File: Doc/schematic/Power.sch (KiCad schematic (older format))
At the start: 19 parts, among them K1 RELAY_1RT, K2 RELAY_1RT, P1 Power Board, P5 Trafo_IN_1, P6 Trafo_IN_2, P7 +24_PWR, Q1 BC548, U2 7805

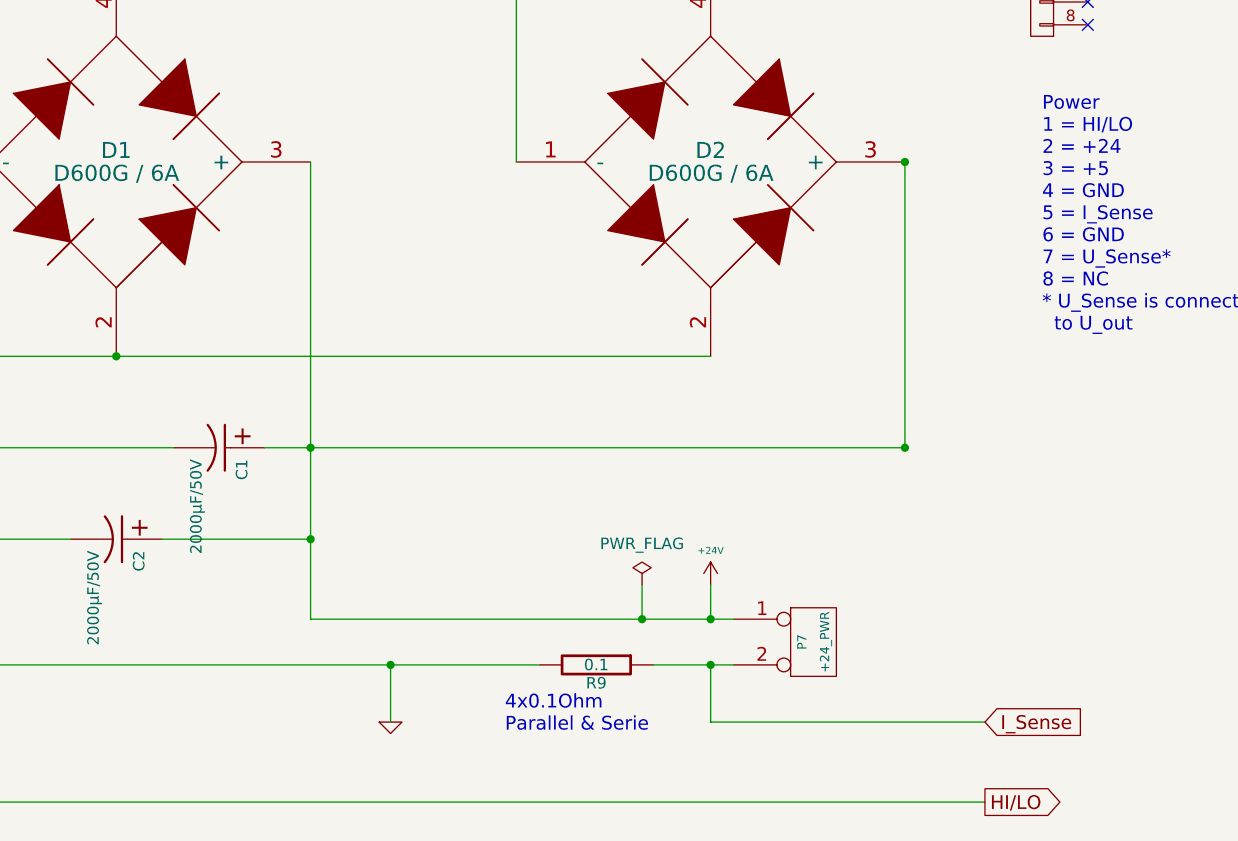
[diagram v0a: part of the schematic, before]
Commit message: Measurements and measurement-display first version finished.
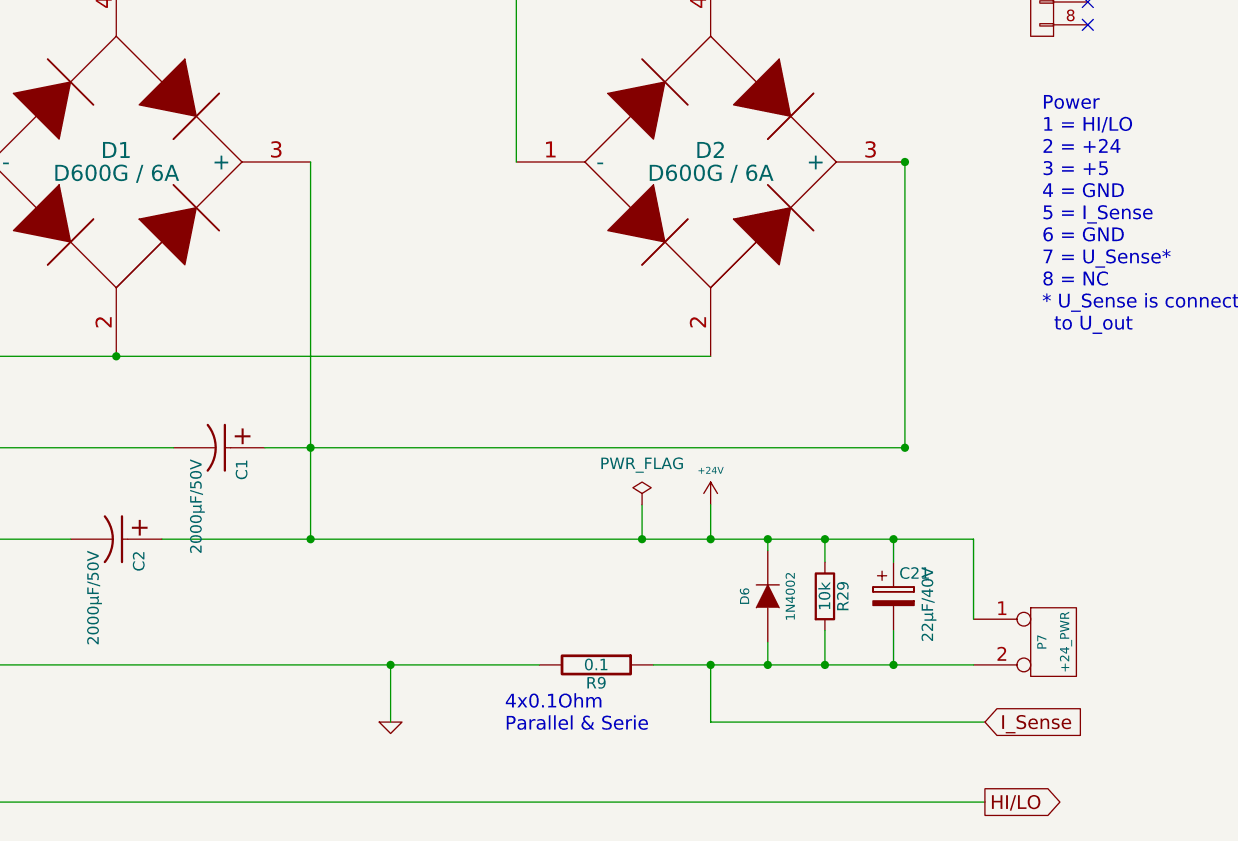
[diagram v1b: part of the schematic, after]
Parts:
- added C21: 22µF/40V, symbol CP
- added D6: 1N4002, symbol DIODE
- added R29: 10k, symbol R
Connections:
- net +24V: now also C21.1, D6.2 (K), R29.1
- net I_Sense: now also C21.2, D6.1 (A), R29.2
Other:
- moved on the sheet: P7
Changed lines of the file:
@@
 	9100 3350 9100 2100
 Wire Wire Line
-	6500 2100 6500 4100
+	6500 2100 6500 3750
 Wire Wire Line
 	4800 1150 4800 4300
@@
 	3350 1000 3350 1700
 Wire Wire Line
-	5850 3750 6500 3750
+	5850 3750 9400 3750
 Connection ~ 5650 1000
 Wire Wire Line
@@
 Wire Wire Line
 	6850 4550 6850 4300
-Wire Wire Line
-	6500 4100 8350 4100
 Wire Wire Line
 	1700 5400 2300 5400
@@
 Connection ~ 2100 2600
 Wire Wire Line
-	8000 4300 8350 4300
+	8000 4300 9400 4300
 Wire Wire Line
 	9450 4550 8250 4550
@@
 $EndComp
 $Comp
-L +24V #PWR22
+L +24V #PWR21
 U 1 1 50201F43
-P 8250 3950
-F 0 "#PWR22" H 8250 3900 20  0001 C CNN
-F 1 "+24V" H 8250 4100 30  0000 C CNN
-F 2 "" H 8250 3950 60  0001 C CNN
-F 3 "" H 8250 3950 60  0001 C CNN
-	1    8250 3950
+P 8250 3600
+F 0 "#PWR21" H 8250 3550 20  0001 C CNN
+F 1 "+24V" H 8250 3750 30  0000 C CNN
+F 2 "" H 8250 3600 60  0001 C CNN
+F 3 "" H 8250 3600 60  0001 C CNN
+	1    8250 3600
 	1    0    0    -1
 $EndComp
@@
 $EndComp
 $Comp
-L GND-RESCUE-Netzteil_Progammable #PWR21
+L GND-RESCUE-Netzteil_Progammable #PWR22
 U 1 1 50201970
 P 2100 3700
-F 0 "#PWR21" H 2100 3700 30  0001 C CNN
+F 0 "#PWR22" H 2100 3700 30  0001 C CNN
 F 1 "GND" H 2100 3630 30  0001 C CNN
 F 2 "" H 2100 3700 60  0001 C CNN
@@
 L CONN_2 P7
 U 1 1 50201731
-P 8700 4200
-F 0 "P7" V 8650 4200 40  0000 C CNN
-F 1 "+24_PWR" V 8750 4200 40  0000 C CNN
-F 2 "" H 8700 4200 60  0001 C CNN
-F 3 "" H 8700 4200 60  0001 C CNN
-	1    8700 4200
+P 9750 4200
+F 0 "P7" V 9700 4200 40  0000 C CNN
+F 1 "+24_PWR" V 9800 4200 40  0000 C CNN
+F 2 "" H 9750 4200 60  0001 C CNN
+F 3 "" H 9750 4200 60  0001 C CNN
+	1    9750 4200
 	1    0    0    -1
 $EndComp
@@
 L PWR_FLAG #FLG2
 U 1 1 589D1F88
-P 7950 3950
-F 0 "#FLG2" H 7950 4045 50  0001 C CNN
-F 1 "PWR_FLAG" H 7950 4130 50  0000 C CNN
-F 2 "" H 7950 3950 50  0000 C CNN
-F 3 "" H 7950 3950 50  0000 C CNN
-	1    7950 3950
+P 7950 3600
+F 0 "#FLG2" H 7950 3695 50  0001 C CNN
+F 1 "PWR_FLAG" H 7950 3780 50  0000 C CNN
+F 2 "" H 7950 3600 50  0000 C CNN
+F 3 "" H 7950 3600 50  0000 C CNN
+	1    7950 3600
 	1    0    0    -1
 $EndComp
@@
 I_Sense
 Wire Wire Line
-	8250 3950 8250 4100
-Connection ~ 8250 4100
-Wire Wire Line
-	7950 3950 7950 4100
-Connection ~ 7950 4100
+	8250 3750 8250 3600
+Connection ~ 8250 3750
+Wire Wire Line
+	7950 3600 7950 3750
+Connection ~ 7950 3750
 NoConn ~ 9900 1400
 Wire Wire Line
 	8750 5950 8750 6050
+Wire Wire Line
+	9400 3750 9400 4100
+$Comp
+L DIODE D6
+U 1 1 58FF4F3C
+P 8500 4000
+F 0 "D6" H 8500 4100 40  0000 C CNN
+F 1 "1N4002" H 8500 3900 40  0000 C CNN
+F 2 "" H 8500 4000 60  0000 C CNN
+F 3 "" H 8500 4000 60  0000 C CNN
+	1    8500 4000
+	0    -1   -1   0
+$EndComp
+$Comp
+L R R29
+U 1 1 58FF4FDD
+P 8750 4000
+F 0 "R29" V 8830 4000 50  0000 C CNN
+F 1 "10k" V 8750 4000 50  0000 C CNN
+F 2 "" V 8680 4000 50  0001 C CNN
+F 3 "" H 8750 4000 50  0001 C CNN
+	1    8750 4000
+	1    0    0    -1
+$EndComp
+$Comp
+L CP C21
+U 1 1 58FF5267
+P 9050 4000
+F 0 "C21" H 9075 4100 50  0000 L CNN
+F 1 "22µF/40V" V 9200 3800 50  0000 L CNN
+F 2 "" H 9088 3850 50  0001 C CNN
+F 3 "" H 9050 4000 50  0001 C CNN
+	1    9050 4000
+	1    0    0    -1
+$EndComp
+Wire Wire Line
+	9050 3850 9050 3750
+Connection ~ 9050 3750
+Wire Wire Line
+	8750 3850 8750 3750
+Connection ~ 8750 3750
+Wire Wire Line
+	8500 3800 8500 3750
+Connection ~ 8500 3750
+Wire Wire Line
+	8500 4200 8500 4300
+Connection ~ 8500 4300
+Wire Wire Line
+	8750 4150 8750 4300
+Connection ~ 8750 4300
+Wire Wire Line
+	9050 4150 9050 4300
+Connection ~ 9050 4300
 $EndSCHEMATC

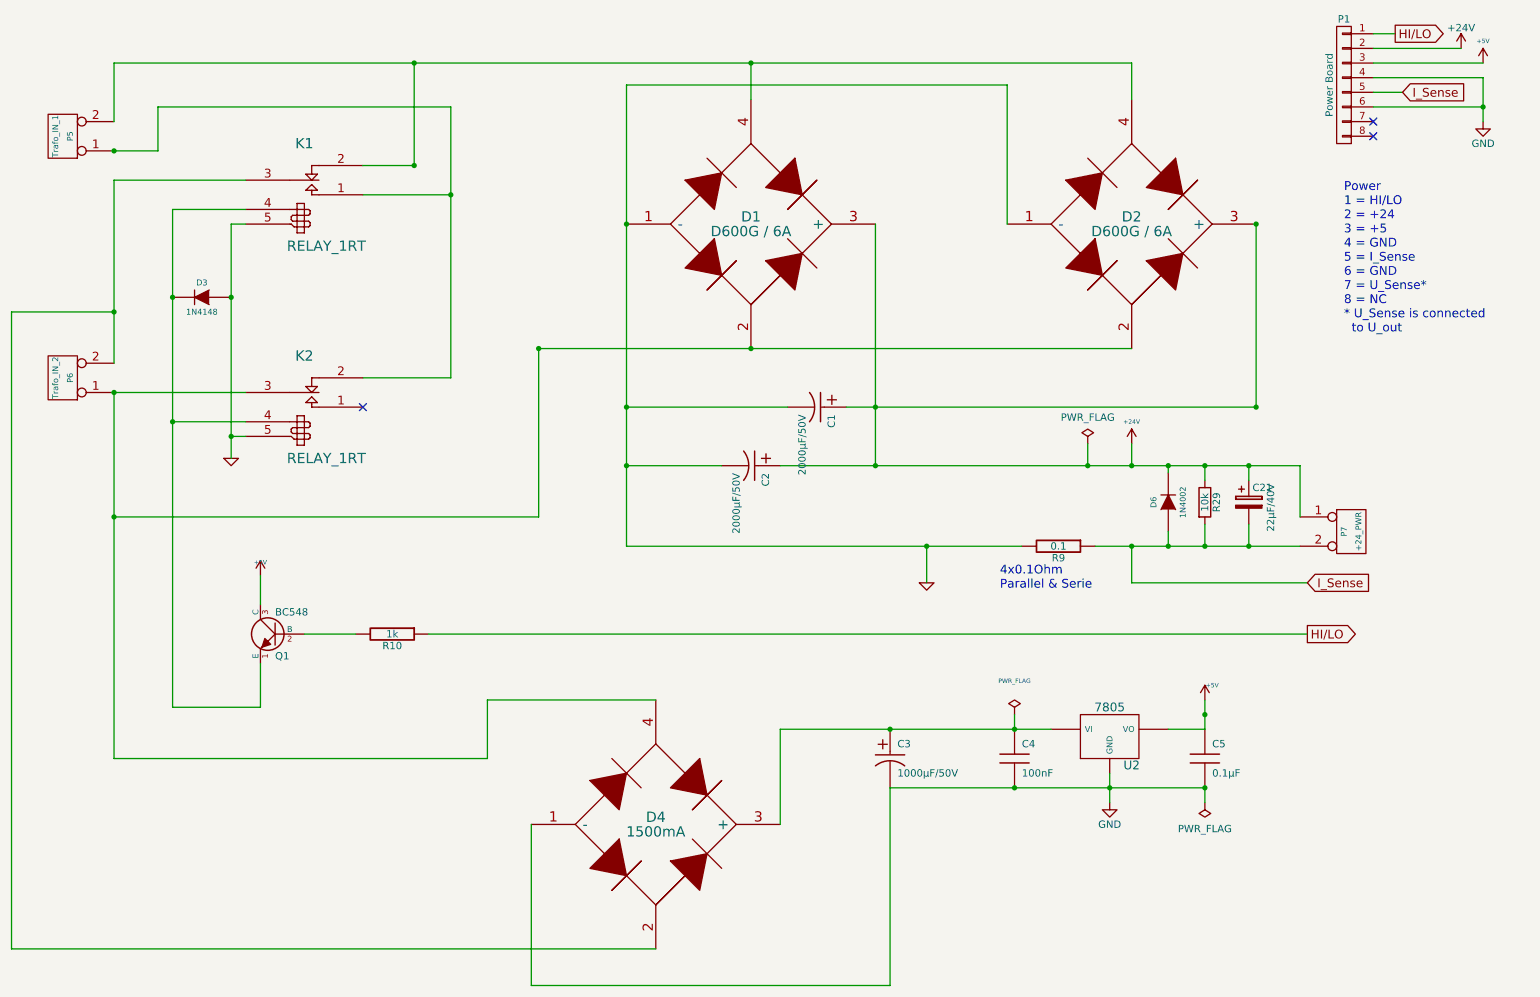
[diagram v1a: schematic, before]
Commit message: Outputting voltage works. Measurement voltage works, not yet calibrated.
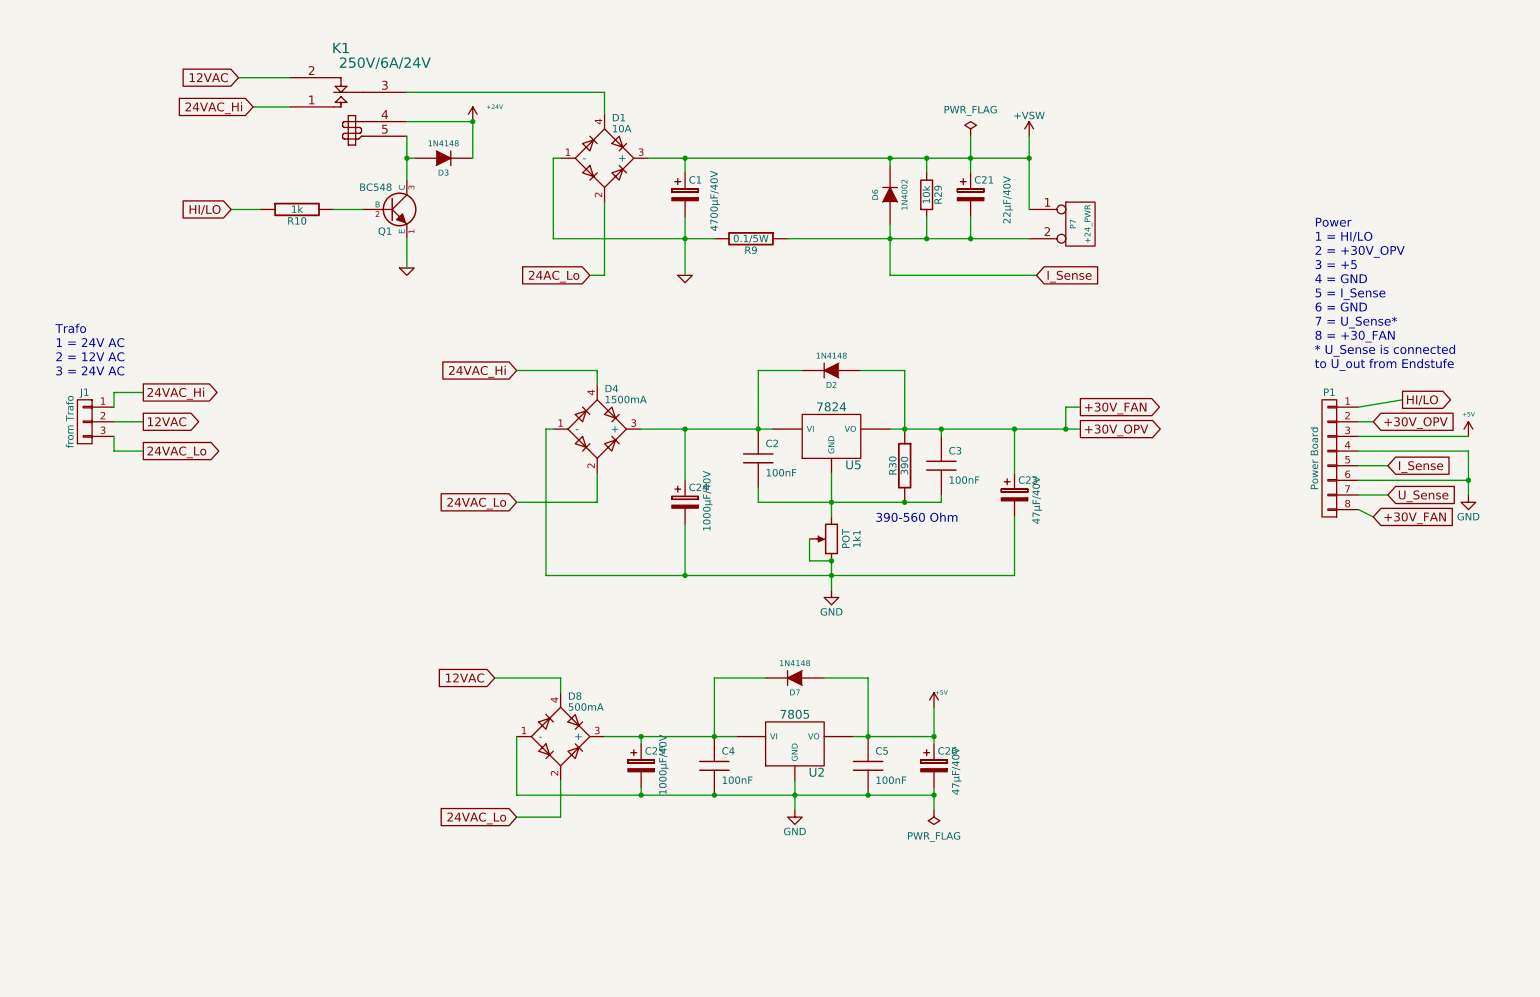
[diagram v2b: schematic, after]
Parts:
- removed C1, C2: 2000µF/50V, symbol CP1-RESCUE-Netzteil_Progammable
- removed C3: 1000µF/50V, symbol CP1-RESCUE-Netzteil_Progammable
- removed D1, D2: D600G / 6A, symbol BRIDGE
- removed D4: 1500mA, symbol BRIDGE
- removed K2: RELAY_1RT, symbol RELAY_1RT
- removed P5: Trafo_IN_1, symbol CONN_2
- removed P6: Trafo_IN_2, symbol CONN_2
- added 1k1: POT, symbol POT
- added C1: 4700µF/40V, symbol CP
- added C2, C3: 100nF, symbol C-RESCUE-Netzteil_Progammable
- added C23, C26: 47µF/40V, symbol CP
- added C24, C25: 1000µF/40V, symbol CP
- added D1: 10A, symbol D_Bridge_-A+A
- added D2, D7: 1N4148, symbol DIODE
- added D4: 1500mA, symbol D_Bridge_-A+A
- added D8: 500mA, symbol D_Bridge_-A+A
- added J1: from Trafo, symbol CONN_01X03
- added R30: 390, symbol R-RESCUE-Netzteil_Progammable
- added U5: 7824, symbol 7805
- C5: value 0.1µF -> 100nF
- K1: value RELAY_1RT -> 250V/6A/24V
- R9: value 0.1 -> 0.1/5W
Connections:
- net +24V: now also D3.2 (K), K1.4 (8); no longer C21.1, D6.2 (K), P1.2 (P2), P7.1 (P1), R29.1
- net +5V: now also C26.1, D7.1 (A); no longer Q1.3 (C)
- net GND: now also Q1.1 (E), 1k1.1, 1k1.2, C1.2, C23.2, C24.2, C25.2, C26.2, D1.1 (-), D4.1 (-), D8.1 (-); no longer D3.1 (A), K1.5
- net 24VAC_Hi: now reaches K1.1 (T1)
- net 24VAC_Hi: now also D4.4, J1.1 (P1)
- net 12VAC: now reaches K1.2 (R1)
- net 12VAC: now also D8.4, J1.2 (P2)
- net at K1.3 (C1): now also D1.4
- net at C4.1, U2.VI: now also C25.1, D7.2 (K), D8.3 (+)
- net U_Sense: now reaches P1.7 (P7)
- net +30V_FAN: now reaches P1.8 (P8)
- net +30V_FAN: now also P1.2 (P2), C23.1, C3.1, D2.1 (A), R30.1, U5.VO
- new net: D3.1 (A), K1.5, Q1.3 (C)
- new net: 1k1.3, C2.2, C3.2, R30.2, U5.GND
- new net: C2.1, C24.1, D2.2 (K), D4.3 (+), U5.VI
- new net +VSW: C1.1, C21.1, D1.3 (+), D6.2 (K), P7.1 (P1), R29.1
- new net 24AC_Lo: D1.2
- new net 24VAC_Lo: D4.2, D8.2, J1.3 (P3)
- no-connect marks 3 -> 0
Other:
- note added: "390-560 Ohm"
- note added: "Power\n1 = HI/LO\n2 = +30V_OPV\n3 = +5\n4 = GND\n5 = I_Sense\n6 = GND\n7 = U_Sense*\n8 = +30_FAN\n* U_Sense is connected\nto U_out from Endstufe"
- note added: "Trafo\n1 = 24V AC\n2 = 12V AC\n3 = 24V AC"
- note removed: "4x0.1Ohm\nParallel & Serie"
- note removed: "Power\n1 = HI/LO\n2 = +24\n3 = +5\n4 = GND\n5 = I_Sense\n6 = GND\n7 = U_Sense*\n8 = NC\n* U_Sense is connected \n to U_out"
- moved on the sheet: C21, C4, C5, D3, D6, K1, P7, Q1, R10, R29, R9, U2
